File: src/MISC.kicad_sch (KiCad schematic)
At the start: 26 parts, among them K1 G6K-2F-Y-TR DC5, K2 G6K-2F-Y-TR DC5, Q14 SI2308A, Q15 SI2308A, Q16 SI2308A, Q17 SI2308A

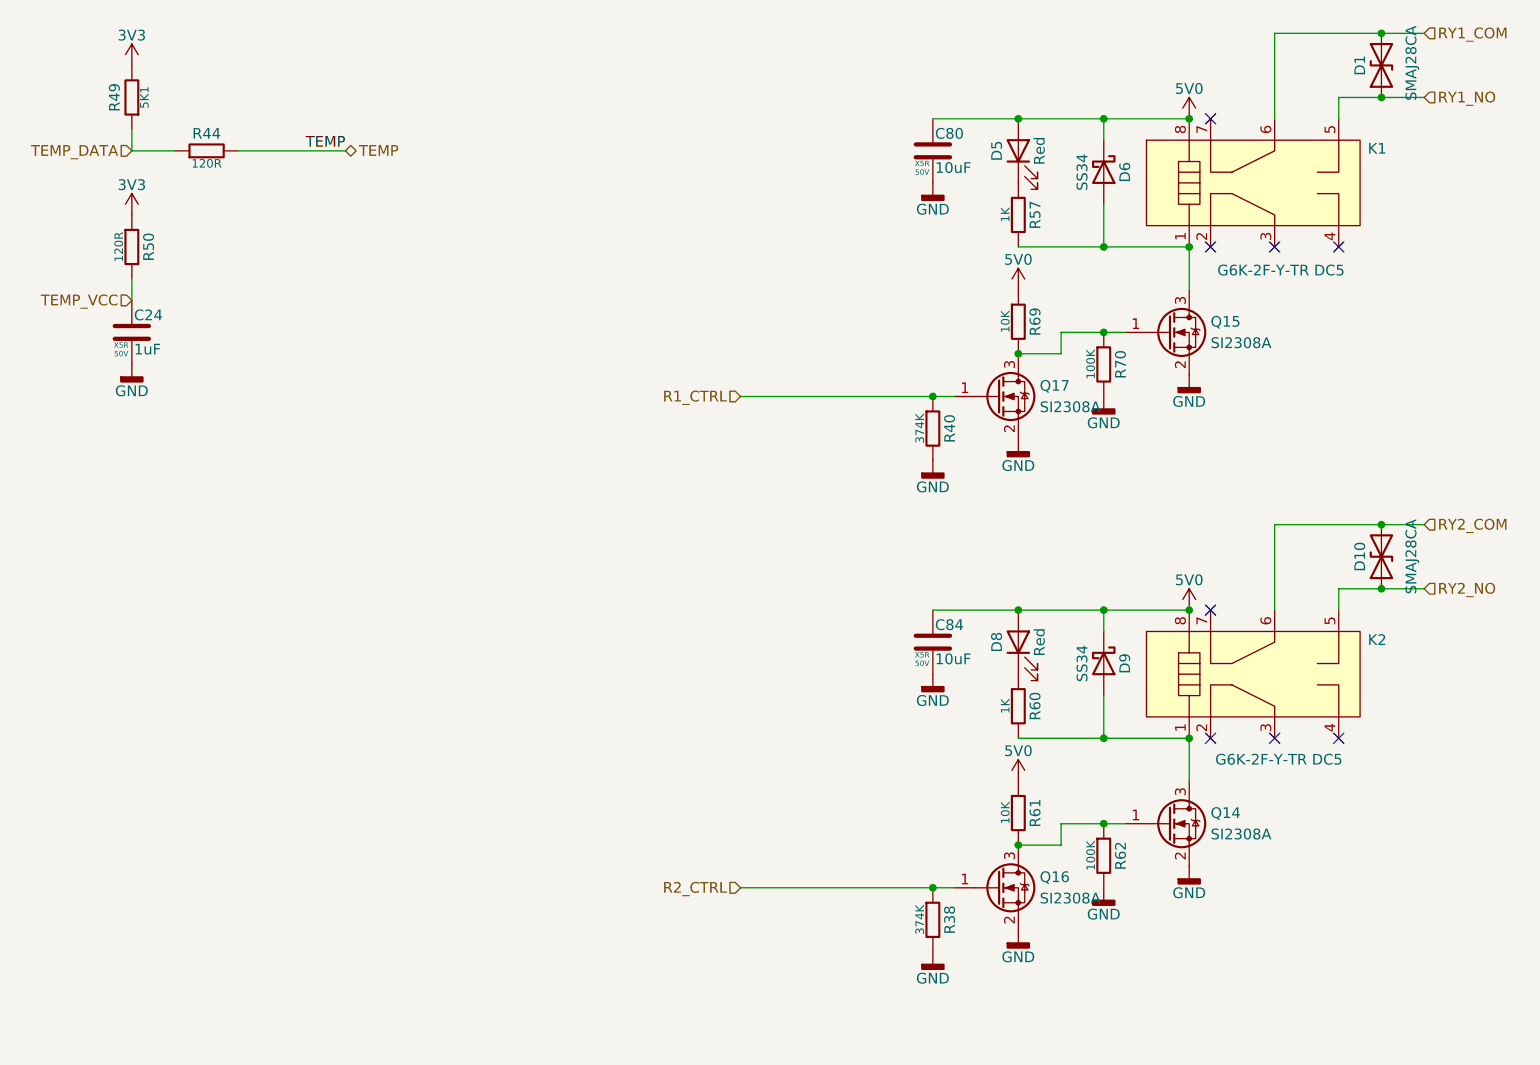
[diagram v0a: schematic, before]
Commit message: Update PCB layout and schematics; add enclosure design files
Bump firmware submodule to WAN failover scenario-audit hardening +
zombie-LTE self-heal (round 2).

Co-Authored-By: Claude Sonnet 5 <noreply@anthropic.com>
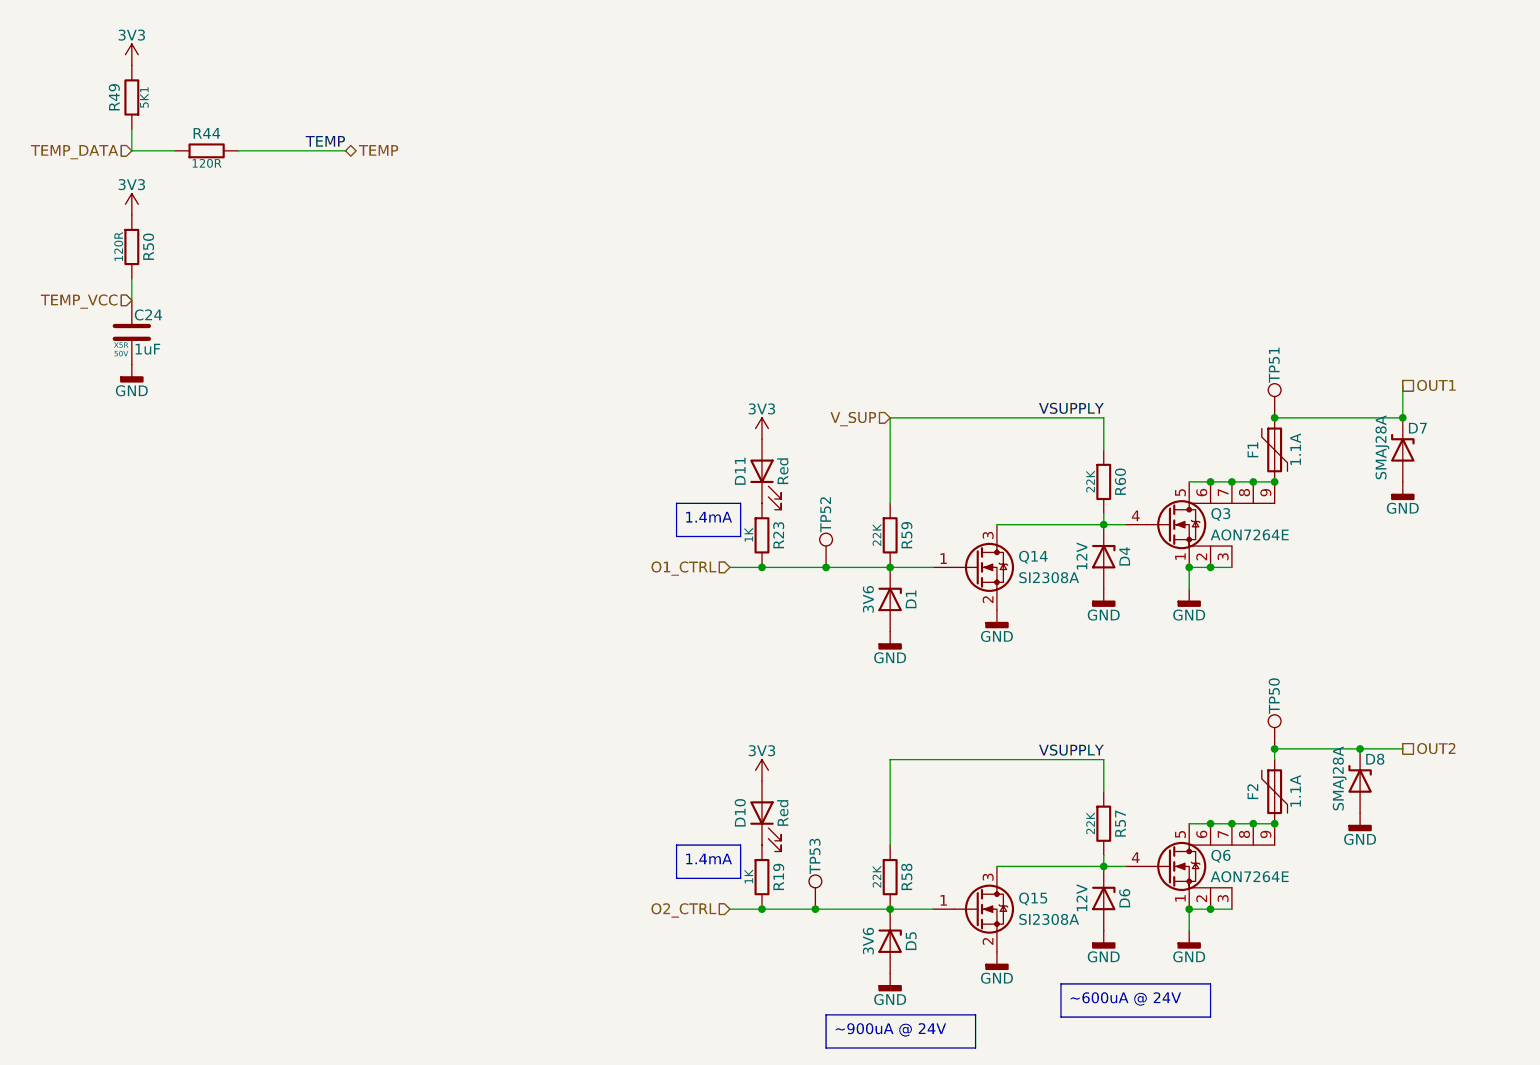
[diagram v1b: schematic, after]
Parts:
- removed C80, C84: 10uF, 7Sigma:C_0805_2012Metric, symbol Capacitor:GRM21BR61H106KE43L
- removed D1, D10: SMAJ28CA, 7Sigma:D_SMA, symbol Diodes:SMAJ28CA
- removed D5, D8: LTST-C281KRKT, 7Sigma:LED_0402_1005Metric, symbol LEDs:LTST-C281KRKT
- removed D6, D9: SS34, 7Sigma:D_SMA, symbol Diodes:SS34
- removed K1, K2: G6K-2F-Y-TR DC5, 7Sigma:RELAY-SMD_G6K-2F-X-XX, symbol Relays:G6K-2F-Y-TR DC5
- removed Q16, Q17: SI2308A, 7Sigma:SOT-23-3, symbol Transistors:SI2308A
- removed R38, R40: 374K, 7Sigma:R_0402_1005Metric, symbol Resistor:0402WGF3743TCE
- removed R57, R60: 1K, 7Sigma:R_0402_1005Metric, symbol Resistor:0402WGF1001TCE
- removed R61, R69: 10K, 7Sigma:R_0402_1005Metric, symbol Resistor:0402WGF1002TCE
- removed R62, R70: 100K, 7Sigma:R_0402_1005Metric, symbol Resistor:0402WGF1003TCE
- added D1, D5: 3V6, 7Sigma:D_SOD-323, symbol Diodes:BZX384-C3V6,115
- added D10, D11: LTST-C281KRKT, 7Sigma:LED_0402_1005Metric, symbol LEDs:LTST-C281KRKT
- added D4, D6: 12V, 7Sigma:D_SOD-323, symbol Diodes:BZX384-C12,115
- added D7, D8: SMAJ28A, 7Sigma:D_SMA, symbol Diodes:SMAJ28A
- added F1, F2: 1.1A, 7Sigma:Fuse_1206_3216Metric, symbol Circuit_Protection:BSMD1206-110-30V
- added Q3, Q6: AON7264E, 7Sigma:DFN-8-1EP_3x3mm_P0.65mm_EP1.55x2.4mm, symbol Transistors:AON7264E
- added R19, R23: 1K, 7Sigma:R_0402_1005Metric, symbol Resistor:0402WGF1001TCE
- added R57, R58, R59, R60: 22K, 7Sigma:R_0402_1005Metric, symbol Resistor:0402WGF2202TCE
- added TP50, TP51, TP52, TP53: TestPoint, 7Sigma:TestPoint_Pad_D1.5mm, symbol TestPoints:TestPoint_Pad_D1.5mm
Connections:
- net 3V3: now also D10.2 (A), D11.2 (A)
- net GND: now also D1.2 (A), D4.2 (A), D5.2 (A), D6.2 (A), D7.2 (A), D8.2 (A), Q3.1 (S), Q3.2 (S), Q3.3 (S), Q6.1 (S), Q6.2 (S), Q6.3 (S)
- net O2_CTRL: now reaches Q15.1 (G)
- net O2_CTRL: now also D5.1 (K), R19.2, R58.2, TP53.1
- net at Q15.3 (D): now also D6.1 (K), Q6.4 (G), R57.2
- net O1_CTRL: now reaches Q14.1 (G)
- net O1_CTRL: now also D1.1 (K), R23.2, R59.2, TP52.1
- net at Q14.3 (D): now also D4.1 (K), Q3.4 (G), R60.2
- new net: D10.1 (K), R19.1
- new net: D11.1 (K), R23.1
- new net: F1.2, Q3.5 (D), Q3.6 (D), Q3.7 (D), Q3.8 (D), Q3.9 (D)
- new net: F2.2, Q6.5 (D), Q6.6 (D), Q6.7 (D), Q6.8 (D), Q6.9 (D)
- new net OUT1: D7.1 (C), F1.1, TP51.1
- new net OUT2: D8.1 (C), F2.1, TP50.1
- new net V_SUP: R57.1, R58.1, R59.1, R60.1
- no-connect marks 8 -> 0
